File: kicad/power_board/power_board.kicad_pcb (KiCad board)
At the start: 2 copper layers, 151 x 77 mm, 58 parts, among them J1 24V, J2 5V, J3 3V3, J4 GND, J6 Grid, J7 MCU, J8 Solar Panel, Q1 FDD8453LZ, Q2 FDD8453LZ, Q3 FDD8453LZ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

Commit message: traffic lights WIP
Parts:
- removed C1, C3: 100uF, Capacitor_THT:C_Radial_D8.0mm_H11.5mm_P3.50mm
- removed C2, C4: 330uF, Capacitor_THT:CP_Radial_D8.0mm_P3.50mm
- removed D2: VS-30WQ04FNTR-M3, Package_TO_SOT_SMD:TO-252-2
- removed L1, L2: 330uH, Inductor_THT:L_Toroid_Vertical_L31.8mm_W15.9mm_P13.50mm_Bourns_5700
- removed U1: LM2575D2T-3.3R4G, Package_TO_SOT_SMD:TO-263-5_TabPin3
- removed U2: LM2575D2T-5R4G, Package_TO_SOT_SMD:TO-263-5_TabPin3
- added J10: Grid, Connector_PinHeader_2.54mm:PinHeader_1x01_P2.54mm_Vertical, F.Cu at (149.4, 61.0)
- added J11: 24V Solar, Connector_PinHeader_2.54mm:PinHeader_1x01_P2.54mm_Vertical, F.Cu at (109.9, 107.6)
- added J5: GND, Connector_PinHeader_2.54mm:PinHeader_1x01_P2.54mm_Vertical, F.Cu at (142.0, 61.0)
- added J9: Solar Panel, _mine:73099, F.Cu at (106.5, 60.0)
- added R1: 1k, Resistor_SMD:R_2512_6332Metric, F.Cu at (122.8, 110.0)
- D1: value VS-30WQ04FNTR-M3 -> LED; footprint Package_TO_SOT_SMD:TO-252-2 -> Capacitor_SMD:C_0603_1608Metric
- J2: value 5V -> 24V
- J3: value 3V3 -> GND
- J4: footprint Connector_PinHeader_2.54mm:PinHeader_1x03_P2.54mm_Vertical -> Connector_PinHeader_2.54mm:PinHeader_1x01_P2.54mm_Vertical
- J6: value Grid -> GND; footprint Connector_PinHeader_2.54mm:PinHeader_1x02_P2.54mm_Vertical -> Connector_PinHeader_2.54mm:PinHeader_1x01_P2.54mm_Vertical
- J8: value Solar Panel -> GND; footprint Connector_PinHeader_2.54mm:PinHeader_1x02_P2.54mm_Vertical -> _mine:73099
- moved J3 109.6 mm to (122.0, 120.0), turned to 0 degrees
- moved J2 102.3 mm to (132.4, 117.5), turned to 0 degrees
- moved D1 72.9 mm to (129.4, 110.0), turned to 0 degrees
- moved J6 68.9 mm to (113.0, 120.0), turned to 0 degrees
- moved J4 63.7 mm to (157.0, 61.0)
- moved H1 50.0 mm to (170.0, 55.0)
- moved H3 50.0 mm to (170.0, 122.0)
- moved C20 6.30 mm to (162.1, 93.8)
- moved C21 6.25 mm to (161.0, 105.2)
- moved J1 5.89 mm to (139.0, 117.5), turned to 0 degrees
- moved J8 3.31 mm to (124.5, 60.0), turned to 0 degrees
- moved J7 3.09 mm to (138.0, 61.0)
- moved H2 3.00 mm to (82.0, 122.0)
- moved H4 3.00 mm to (82.0, 55.0)
- moved C22 0.85 mm to (149.2, 109.3)
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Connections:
- D1 pad 2: GND -> +24V
- J2 pad 1: +5V -> +24V
- J3 pad 1: +3V3 -> GND
- J6 pad 1: 24V Grid -> GND
- J8 pad 1: Solar Panel -> GND
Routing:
- net +5V: track 87.5 -> 0.00 mm
- net +3V3: track 59.5 -> 0.00 mm
- net Net-(D1-Pad1): track 49.0 -> 2.86 mm
- net GND: track 49.3 -> 21.4 mm, vias 23 -> 20
- net +24V: track 23.6 -> 0.00 mm
- net Net-(D2-Pad1): track 21.4 -> 0.00 mm
- net MCU_SOLAR: track 25.6 -> 24.5 mm
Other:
- board size 151 x 77 mm -> 98.4 x 77 mm

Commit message: WIP
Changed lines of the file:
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@@
         (xy 101.5 84.75)
         (xy 101.5 80.05)
-        (xy 100.34 80.05)
-        (xy 100.34 71.05)
+        (xy 99.86 80.05)
+        (xy 99.86 71.05)
         (xy 103 71.05)
       )
@@
         (xy 108.7 76.35)
         (xy 108.7 71.05)
-        (xy 100.34 71.05)
-        (xy 100.34 68.25)
+        (xy 99.86 71.05)
+        (xy 99.86 68.25)
         (xy 112.35 68.25)
       )

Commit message: light board done
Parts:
- added J12: MCU_2, Connector_PinHeader_2.54mm:PinHeader_1x02_P2.54mm_Vertical, F.Cu at (116.5, 117.5)
- added J13: GND, Connector_PinHeader_2.54mm:PinHeader_1x01_P2.54mm_Vertical, F.Cu at (130.0, 105.0)
- added R2: 0.02, Resistor_SMD:R_0603_1608Metric, F.Cu at (118.7, 103.5)
- added R3: 0, Resistor_SMD:R_2512_6332Metric, F.Cu at (106.5, 105.5)
- added R4: 0, Resistor_SMD:R_2512_6332Metric, F.Cu at (106.5, 115.5)
- added R5: 0, Resistor_SMD:R_2512_6332Metric, F.Cu at (101.5, 105.5)
- added R6: 0, Resistor_SMD:R_2512_6332Metric, F.Cu at (101.5, 115.5)
- added U1: LTC4151xMS, Package_SO:MSOP-10_3x3mm_P0.5mm, F.Cu at (118.8, 107.7)
- moved R1 49.9 mm to (172.5, 106.0), turned to -90 degrees
- moved D1 40.9 mm to (169.2, 100.5), turned to 180 degrees
- moved J3 26.6 mm to (148.5, 117.5)
- moved J11 15.8 mm to (125.5, 105.0)
- moved J6 9.34 mm to (122.0, 117.5)
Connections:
- J11 pad 1: 24V Solar -> 24V Solar_2
- Q4 pad 2: 24V Solar -> 24V Solar_2
- U6 pad 13: 24V Solar -> 24V Solar_2
- U6 pad 15: 24V Solar -> 24V Solar_2
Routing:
- net 24V Solar_2: track 0.00 -> 21.7 mm, vias 0 -> 2
- net Net-(U1-Pad3): track 0.00 -> 20.2 mm
- net 24V Solar: track 17.8 -> 0.45 mm, vias 2 -> 0
- net Net-(R3-Pad2): track 0.00 -> 14.3 mm
- net MCU_SDA: track 0.00 -> 12.8 mm
- net MCU_SCL: track 0.00 -> 10.7 mm
- net GND: track 21.4 -> 26.8 mm, vias 20 -> 24
- net Net-(Q5-Pad1): track 4.34 -> 5.64 mm
- net Net-(D1-Pad1): track 2.86 -> 3.62 mm
- added copper zone on F.Cu, net 24V Solar_2

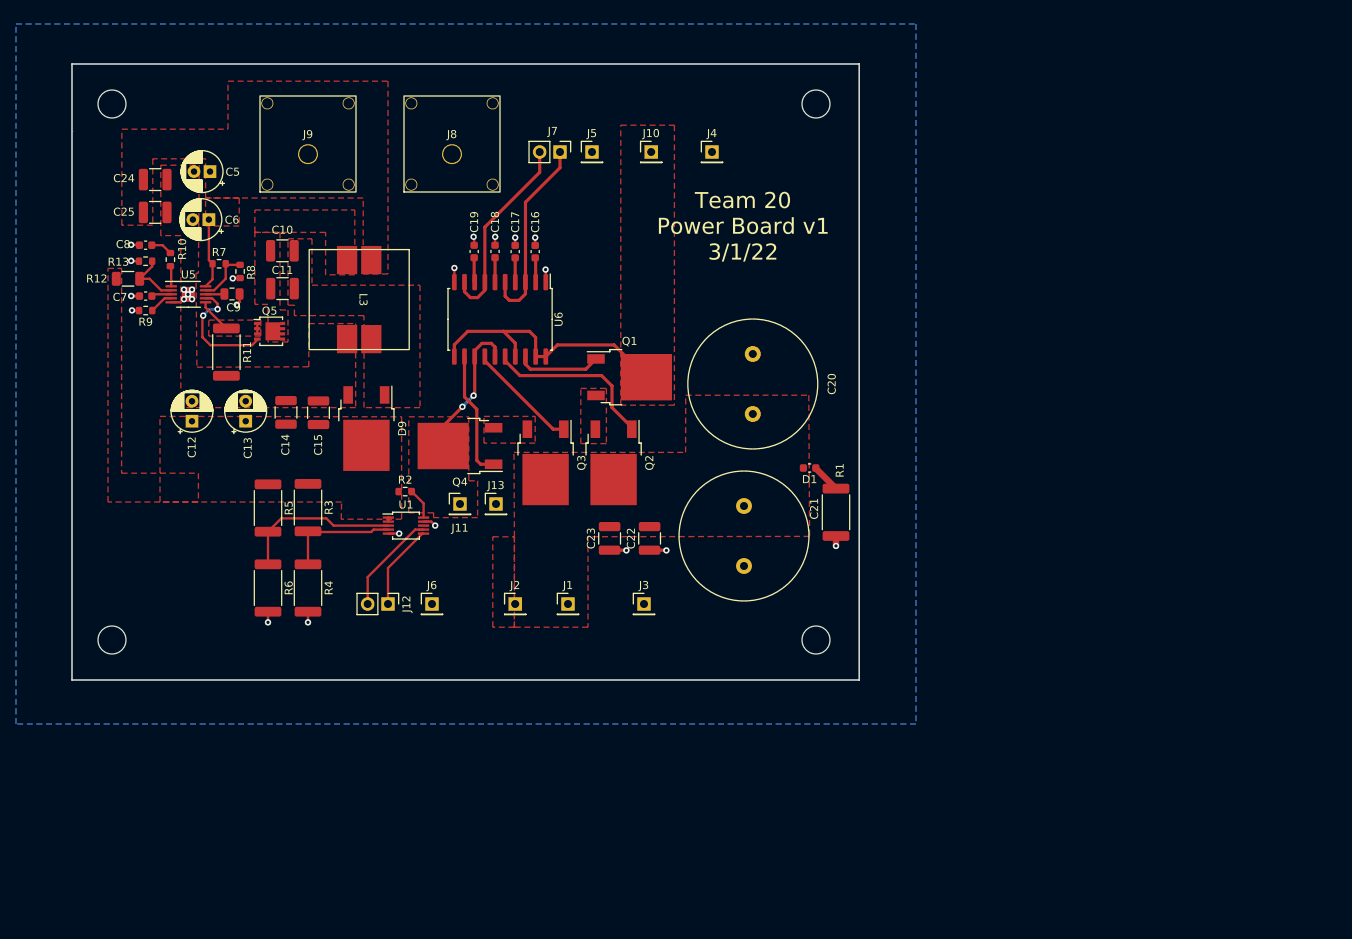
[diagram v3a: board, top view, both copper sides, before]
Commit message: added isolation to power and light boards
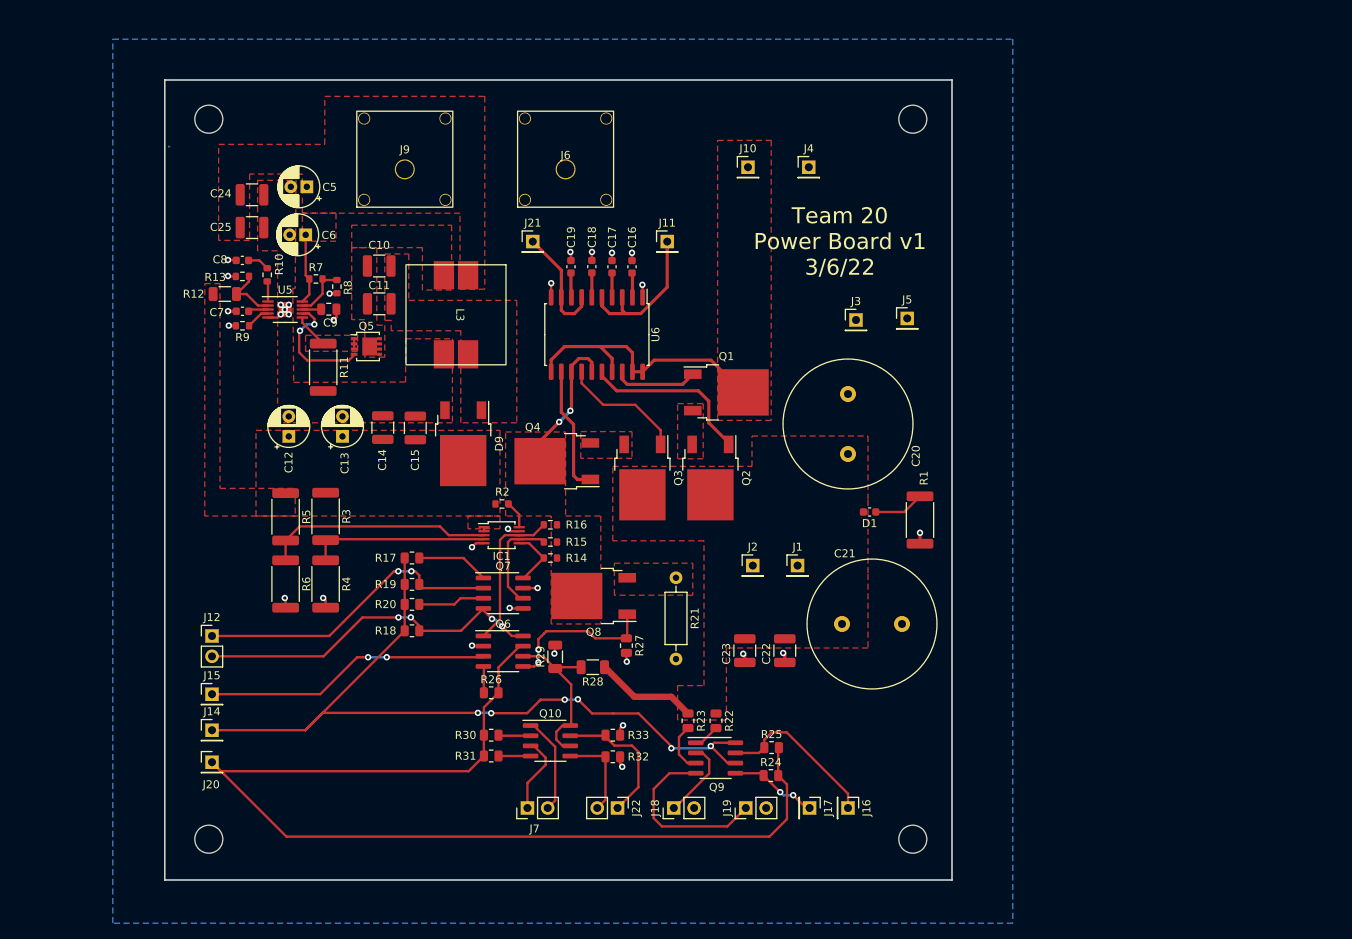
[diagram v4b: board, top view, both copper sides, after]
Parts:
- removed J13: GND, Connector_PinHeader_2.54mm:PinHeader_1x01_P2.54mm_Vertical
- removed J8: GND, _mine:73099
- removed U1: LTC4151xMS, Package_SO:MSOP-10_3x3mm_P0.5mm
- added IC1: LTC4151IMS-1#PBF, Package_SO:MSOP-10_3x3mm_P0.5mm, F.Cu at (130.7, 108.9)
- added J14: 5V, Connector_PinHeader_2.54mm:PinHeader_1x01_P2.54mm_Vertical, F.Cu at (94.5, 133.3)
- added J15: MCU_P_RES, Connector_PinHeader_2.54mm:PinHeader_1x01_P2.54mm_Vertical, F.Cu at (94.5, 128.8)
- added J16: MCU_BTN1, Connector_PinHeader_2.54mm:PinHeader_1x01_P2.54mm_Vertical, F.Cu at (174.0, 143.0)
- added J17: MCU_BTN2, Connector_PinHeader_2.54mm:PinHeader_1x01_P2.54mm_Vertical, F.Cu at (169.2, 143.0)
- added J18: BTN1, Connector_PinHeader_2.54mm:PinHeader_1x02_P2.54mm_Vertical, F.Cu at (152.2, 143.0)
- added J19: BTN2, Connector_PinHeader_2.54mm:PinHeader_1x02_P2.54mm_Vertical, F.Cu at (161.2, 143.0)
- added J20: MCU_GND, Connector_PinHeader_2.54mm:PinHeader_1x01_P2.54mm_Vertical, F.Cu at (94.5, 137.3)
- added J21: SOLAR_CTRL, Connector_PinHeader_2.54mm:PinHeader_1x01_P2.54mm_Vertical, F.Cu at (134.6, 72.2)
- added J22: CTRL, Connector_PinHeader_2.54mm:PinHeader_1x02_P2.54mm_Vertical, F.Cu at (145.2, 143.0)
- added Q10: MOCD207M, Package_SO:SOIC-8_3.9x4.9mm_P1.27mm, F.Cu at (136.8, 134.6)
- added Q6: MOCD207M, Package_SO:SOIC-8_3.9x4.9mm_P1.27mm, F.Cu at (130.9, 123.4)
- added Q7: MOCD207M, Package_SO:SOIC-8_3.9x4.9mm_P1.27mm, F.Cu at (130.9, 116.2)
- added Q8: FDD8453LZ, Package_TO_SOT_SMD:TO-252-2, F.Cu at (142.2, 116.5)
- added Q9: MOCD207M, Package_SO:SOIC-8_3.9x4.9mm_P1.27mm, F.Cu at (157.4, 136.8)
- added R14: 20k, Resistor_SMD:R_0603_1608Metric, F.Cu at (136.8, 111.8)
- added R15: 20k, Resistor_SMD:R_0603_1608Metric, F.Cu at (136.8, 109.8)
- added R16: 5.1k, Resistor_SMD:R_0603_1608Metric, F.Cu at (136.8, 107.6)
- added R17: 0.51k, Resistor_SMD:R_0805_2012Metric, F.Cu at (119.5, 111.8)
- added R18: 10k, Resistor_SMD:R_0805_2012Metric, F.Cu at (119.5, 120.8)
- added R19: 10k, Resistor_SMD:R_0805_2012Metric, F.Cu at (119.5, 115.0)
- added R20: 0.51k, Resistor_SMD:R_0805_2012Metric, F.Cu at (119.5, 117.5)
- added R21: TEH140M33R0FE, Resistor_THT:R_Axial_DIN0207_L6.3mm_D2.5mm_P10.16mm_Horizontal, F.Cu at (152.5, 114.2)
- added R22: 10k, Resistor_SMD:R_0805_2012Metric, F.Cu at (157.5, 132.1)
- added R23: 10k, Resistor_SMD:R_0805_2012Metric, F.Cu at (154.0, 132.1)
- added R24: 10k, Resistor_SMD:R_0805_2012Metric, F.Cu at (164.4, 138.9)
- added R25: 10k, Resistor_SMD:R_0805_2012Metric, F.Cu at (164.4, 135.4)
- added R26: 10k, Resistor_SMD:R_0805_2012Metric, F.Cu at (129.4, 128.6)
- added R27: 10k, Resistor_SMD:R_0805_2012Metric, F.Cu at (146.3, 122.7)
- added R28: 100k, Resistor_SMD:R_1206_3216Metric, F.Cu at (142.1, 125.4)
- added R29: 100k, Resistor_SMD:R_1206_3216Metric, F.Cu at (137.4, 124.1)
- added R30: 10k, Resistor_SMD:R_0805_2012Metric, F.Cu at (129.4, 133.9)
- added R31: 10k, Resistor_SMD:R_0805_2012Metric, F.Cu at (129.4, 136.5)
- added R32: 10k, Resistor_SMD:R_0805_2012Metric, F.Cu at (144.6, 136.6)
- added R33: 10k, Resistor_SMD:R_0805_2012Metric, F.Cu at (144.6, 133.9)
- J11: value 24V Solar -> GRID_CTRL
- J6: footprint Connector_PinHeader_2.54mm:PinHeader_1x01_P2.54mm_Vertical -> _mine:73099
- moved J7 82.1 mm to (133.9, 143.0), turned to 90 degrees
- moved J6 58.1 mm to (138.7, 61.9)
- moved J5 44.6 mm to (181.4, 81.8)
- moved J3 44.3 mm to (175.0, 82.0)
- moved J11 41.8 mm to (151.4, 72.2)
- moved J2 30.1 mm to (162.1, 112.7)
- moved J1 29.1 mm to (167.7, 112.7)
- moved H2 27.7 mm to (94.1, 146.9)
- moved H3 27.7 mm to (182.1, 146.9)
- moved J12 22.4 mm to (94.5, 121.5), turned to 0 degrees
- moved C22 22.0 mm to (166.1, 123.3)
- moved C23 22.0 mm to (161.1, 123.3)
- moved C21 19.2 mm to (173.2, 120.0), turned to 0 degrees
- moved C20 12.9 mm to (174.0, 98.8)
- moved Q1 12.2 mm to (158.8, 91.0)
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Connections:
- net Net-(R3-Pad2) renamed ADR0
- net Net-(U1-Pad3) renamed ADR1
- J11 pad 1: 24V Solar_2 -> Net-(J11-Pad1)
- U6 pad 3: MCU_GRID -> Net-(J11-Pad1)
- U6 pad 5: MCU_GRID -> Net-(J11-Pad1)
- U6 pad 7: MCU_SOLAR -> Net-(J21-Pad1)
- U6 pad 9: MCU_SOLAR -> Net-(J21-Pad1)
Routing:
- net GND1: track 0.00 -> 137.3 mm
- net +5V: track 0.00 -> 100.7 mm, vias 0 -> 6
- net MCU_P_RES: track 0.00 -> 35.9 mm, vias 0 -> 2
- net MCU_SDA: track 12.8 -> 44.7 mm, vias 0 -> 4
- net MCU_SCL: track 10.7 -> 38.8 mm, vias 0 -> 2
- net Net-(J19-Pad1): track 0.00 -> 22.6 mm
- net 12V: track 0.00 -> 21.1 mm
- net MCU_BTN1: track 0.00 -> 20.7 mm
- net Net-(Q6-Pad5): track 0.00 -> 19.9 mm, vias 0 -> 2
- net N_SDAO: track 0.00 -> 19.1 mm
- net Net-(J11-Pad1): track 0.00 -> 18.9 mm
- net SOLAR_CTRL: track 0.00 -> 17.6 mm
- net MCU_GRID: track 24.4 -> 9.72 mm
- net Net-(J21-Pad1): track 0.00 -> 14.3 mm
- net +24V: track 0.00 -> 12.8 mm
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- added copper zone on F.Cu, net Net-(Q8-Pad3)
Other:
- board size 98.4 x 77 mm -> 98.4 x 100 mm
- board text added: "Team 20 Power Board v1 3/6/22"
- board text removed: "Team 20 Power Board v1 3/1/22"
